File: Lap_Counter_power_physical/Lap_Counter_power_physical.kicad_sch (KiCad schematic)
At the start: 26 parts, among them J1 Panel Barrel_Jack, J11 Screw_Terminal_01x04, J18 Screw_Terminal_01x04, J2 Barrel_Jack, J3 Barrel_Plug, J4 Barrel_Jack, J5 Barrel_Plug, J6 Screw_Terminal_01x04, J7 Screw_Terminal_01x04, J8 Screw_Terminal_01x06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

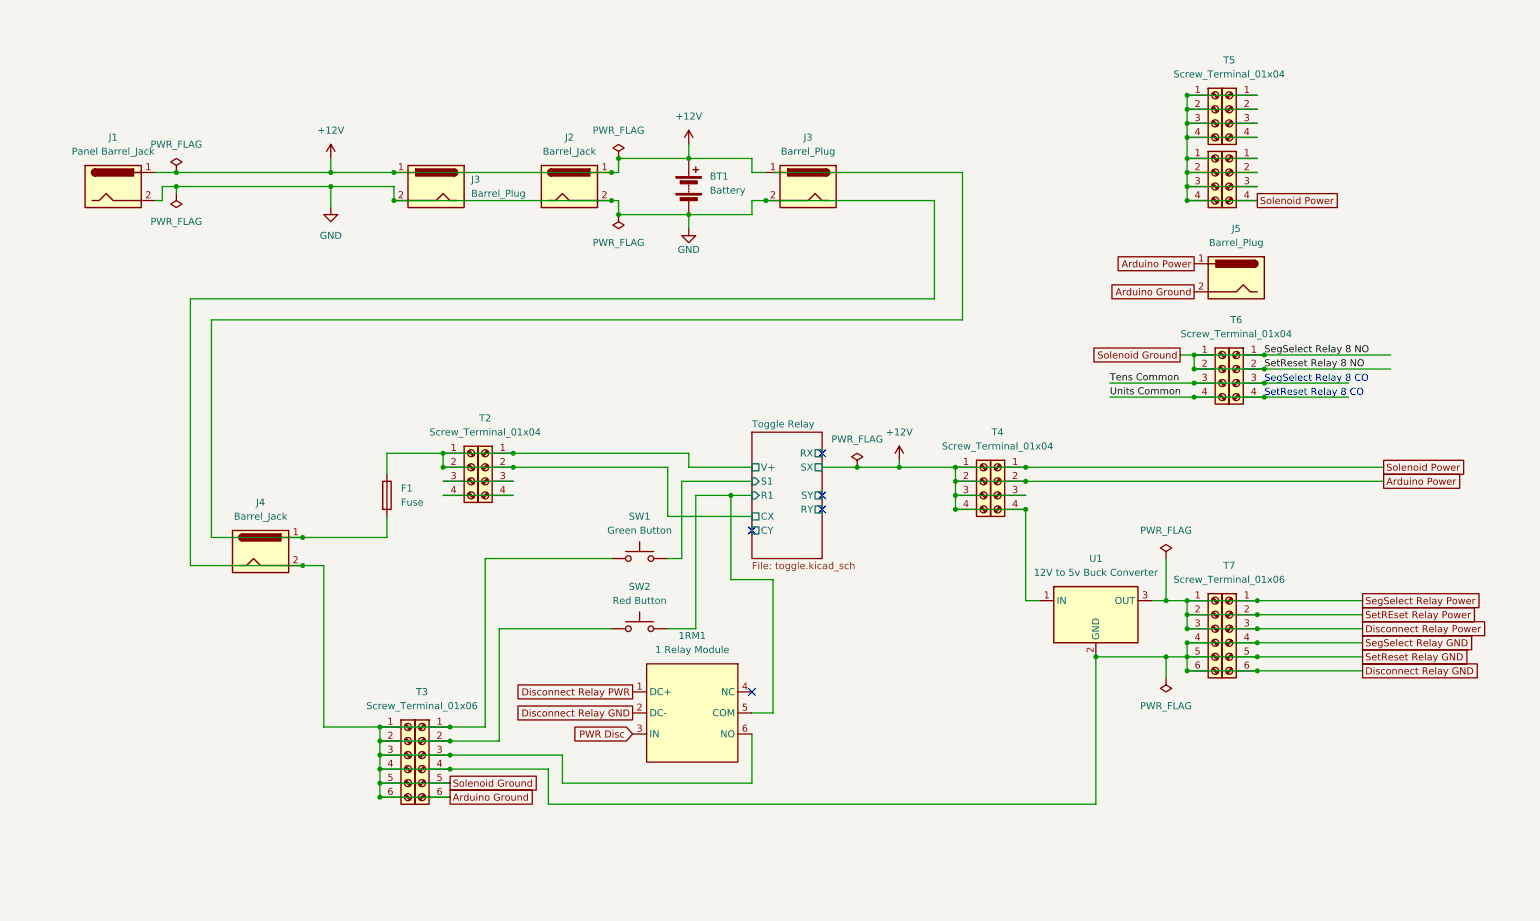
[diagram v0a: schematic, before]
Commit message: Documentation clean up and addition of spec sheets
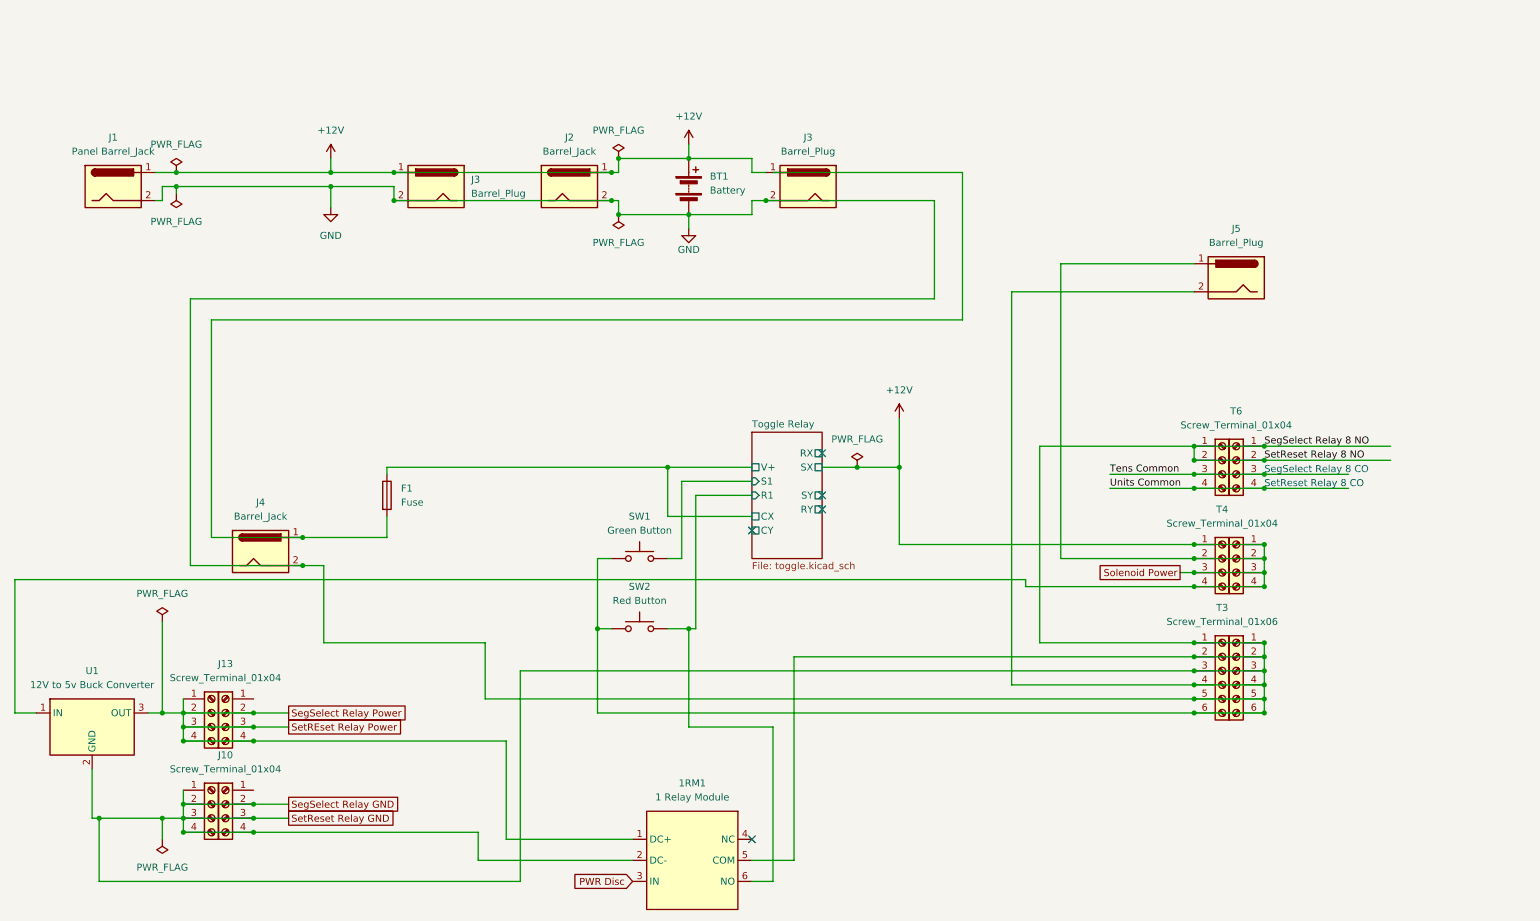
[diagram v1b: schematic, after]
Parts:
- removed J6, J7, T2, T5, T8: Screw_Terminal_01x04, symbol Connector:Screw_Terminal_01x04
- removed T7, T8: Screw_Terminal_01x06, symbol Connector:Screw_Terminal_01x06
- added J10, J12, J13: Screw_Terminal_01x04, symbol Connector:Screw_Terminal_01x04
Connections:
- net Disconnect Relay Power is gone; now on net SegSelect Relay Power: U1.3 (OUT)
- net GND: now also 1RM1.5 (COM), J9.1 (Pin_1), J9.2 (Pin_2), J9.3 (Pin_3), J9.4 (Pin_4), J10.2 (Pin_2), J10.3 (Pin_3), J10.4 (Pin_4); no longer 1RM1.6 (NO)
- net Toggle Relay/CX: no longer J9.1 (Pin_1), J9.2 (Pin_2)
- net Toggle Relay/R1: now also 1RM1.6 (NO); no longer 1RM1.5 (COM)
- net Disconnect Relay PWR renamed SegSelect Relay Power
- net SegSelect Relay Power: now also J12.1 (Pin_1), J12.2 (Pin_2), J12.3 (Pin_3), J12.4 (Pin_4), J13.2 (Pin_2), J13.3 (Pin_3), J13.4 (Pin_4)
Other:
- moved on the sheet: 1RM1, T3, T4, T6, U1

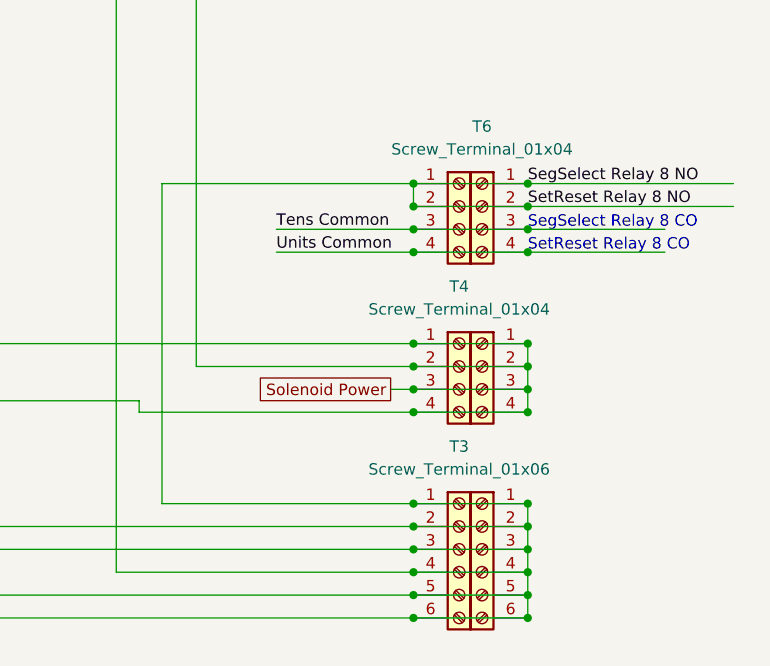
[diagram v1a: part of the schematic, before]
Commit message: eliminate over-large mp4 file
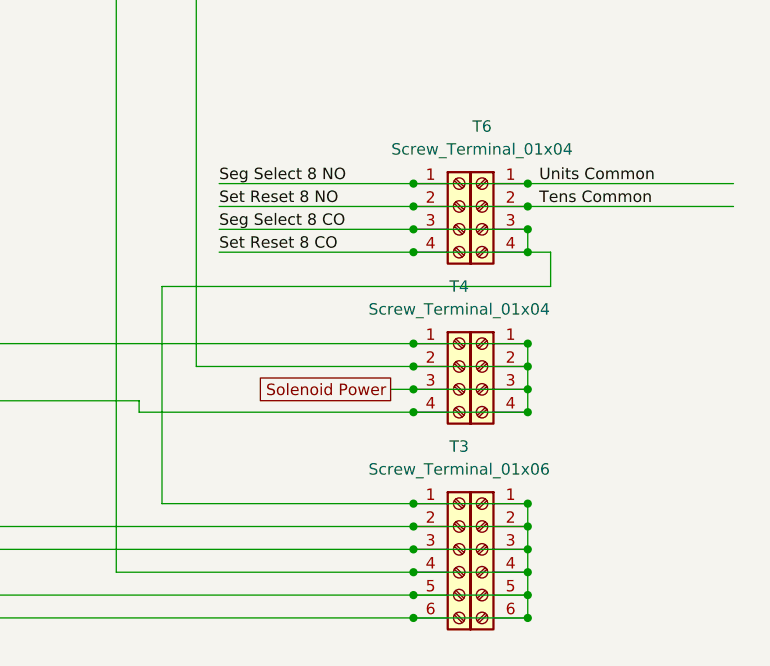
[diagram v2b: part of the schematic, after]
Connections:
- net Tens Common is gone; now on net GND: J18.3 (Pin_3), T6.3 (Pin_3)
- net Units Common is gone; now on net GND: J18.4 (Pin_4), T6.4 (Pin_4)
- net GND: no longer J18.1 (Pin_1), J18.2 (Pin_2), T6.1 (Pin_1), T6.2 (Pin_2)
- new net Seg Select 8 NO: J18.1 (Pin_1), T6.1 (Pin_1)
- new net Set Reset 8 NO: J18.2 (Pin_2), T6.2 (Pin_2)
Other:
- note removed: "SegSelect Relay 8 CO"
- note removed: "SetReset Relay 8 CO"

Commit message: Update documen
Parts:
- added DRC1: DieseRC RC Switch, symbol Project_Library:DieseRC_Remote_Control_Switch
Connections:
- net +12V: now also DRC1. (VCC)
- net GND: now also DRC1. (VCC)
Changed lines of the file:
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@@
 	)
 	(junction
+		(at 189.23 115.57)
+		(diameter 0)
+		(color 0 0 0 0)
+	)
+	(junction
 		(at 228.6 97.79)
 		(diameter 0)
@@
 	)
 	(junction
+		(at 191.77 135.89)
+		(diameter 0)
+		(color 0 0 0 0)
+	)
+	(junction
 		(at 228.6 133.35)
 		(diameter 0)
@@
 	(wire
 		(pts
-			(xy 175.26 115.57) (xy 228.6 115.57)
+			(xy 175.26 115.57) (xy 189.23 115.57)
 		)
 		(stroke
@@
 	(wire
 		(pts
+			(xy 189.23 115.57) (xy 228.6 115.57)
+		)
+		(stroke
+			(width 0)
+			(type default)
+		)
+	)
+	(wire
+		(pts
 			(xy 207.01 105.41) (xy 228.6 105.41)
 		)
@@
 	(wire
 		(pts
+			(xy 191.77 39.37) (xy 191.77 135.89)
+		)
+		(stroke
+			(width 0)
+			(type default)
+		)
+	)
+	(wire
+		(pts
 			(xy 228.6 100.33) (xy 241.3 100.33)
 		)
@@
 	(wire
 		(pts
-			(xy 156.21 135.89) (xy 228.6 135.89)
+			(xy 156.21 135.89) (xy 191.77 135.89)
 		)
 		(stroke
@@
 	(wire
 		(pts
+			(xy 191.77 135.89) (xy 228.6 135.89)
+		)
+		(stroke
+			(width 0)
+			(type default)
+		)
+	)
+	(wire
+		(pts
 			(xy 123.19 48.26) (xy 124.46 48.26)
 		)
@@
 	(wire
 		(pts
+			(xy 189.23 39.37) (xy 189.23 115.57)
+		)
+		(stroke
+			(width 0)
+			(type default)
+		)
+	)
+	(wire
+		(pts
 			(xy 123.19 53.34) (xy 124.46 53.34)
 		)
@@
 					(unit 1)
 				)
+			)
+		)
+	)
+	(symbol
+		(lib_id "Project_Library:DieseRC_Remote_Control_Switch")
+		(at 180.34 21.59 0)
+		(unit 1)
+		(exclude_from_sim no)
+		(in_bom yes)
+		(on_board yes)
+		(dnp no)
+		(fields_autoplaced yes)
+		(property "Reference" "DRC1"
+			(at 195.58 26.6699 0)
+			(effects
+				(font
+					(size 1.27 1.27)
+				)
+				(justify left)
+			)
+		)
+		(property "Value" "DieseRC RC Switch"
+			(at 195.58 29.2099 0)
+			(effects
+				(font
+					(size 1.27 1.27)
+				)
+				(justify left)
+			)
+		)
+		(property "Footprint" ""
+			(at 180.34 21.59 0)
+			(effects
+				(font
+					(size 1.27 1.27)
+				)
+				(hide yes)
+			)
+		)
+		(property "Datasheet" ""
+			(at 180.34 21.59 0)
+			(effects
+				(font
+					(size 1.27 1.27)
+				)
+				(hide yes)
+			)
+		)
+		(property "Description" ""
+			(at 180.34 21.59 0)
+			(effects
+				(font
+					(size 1.27 1.27)
+				)
+				(hide yes)
+			)
+		)
+		(pin "8"
+		)
+		(pin "1"
+		)
+		(pin "4"
+		)
+		(pin "5"
+		)
+		(pin "3"
+		)
+		(pin "11"
+		)
+		(pin "10"
+		)
+		(pin ""
+		)
+		(pin "7"
+		)
+		(pin ""
+		)
+		(pin "6"
+		)
+		(pin "2"
+		)
+		(pin "12"
+		)
+		(pin "9"
+		)
+		(instances
+			(project "Lap_Counter_power_physical"
+				(path "/78a9eac1-cabd-44e7-bd78-57e12cee5a04"
+					(reference "DRC1")
+					(unit 1)
+				)

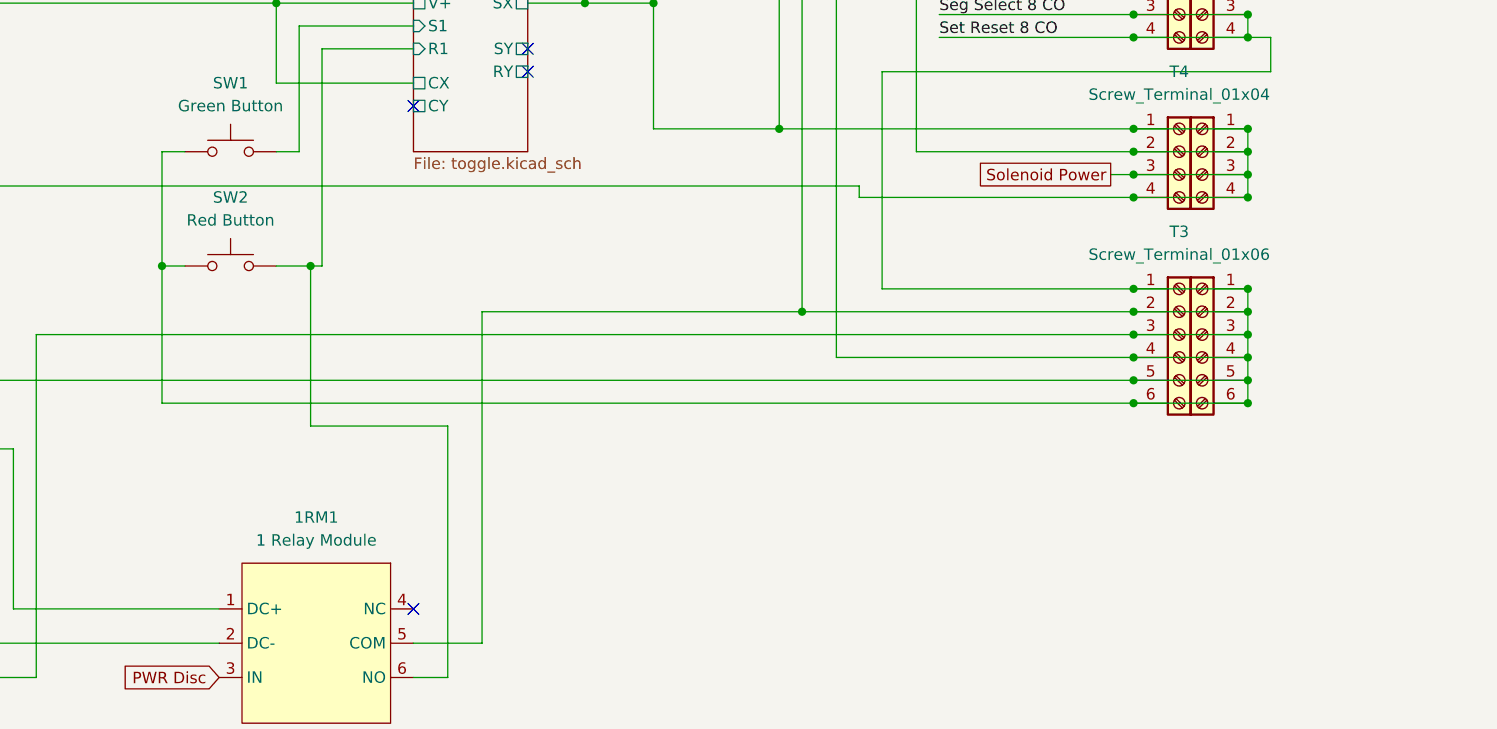
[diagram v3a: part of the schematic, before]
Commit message: Update Documentation for added regulator.
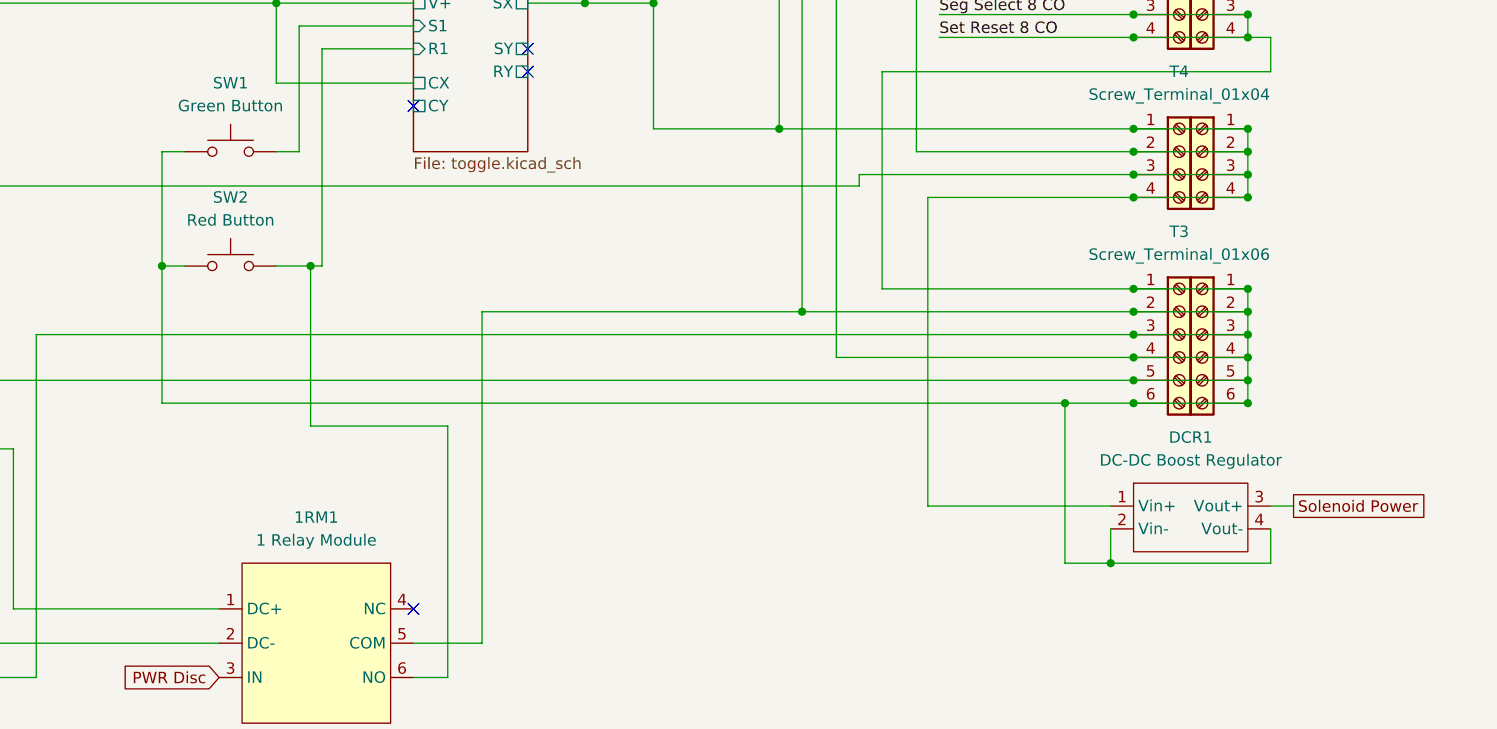
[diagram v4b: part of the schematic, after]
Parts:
- added DCR1: DC-DC Boost Regulator, symbol Project_Library:Ymiko_DC-DC_regulator
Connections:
- net +12V: now also DCR1.1 (Vin+)
- net GND: now also DCR1.2 (Vin-), DCR1.4 (Vout-)
- new net Solenoid Power: DCR1.3 (Vout+)
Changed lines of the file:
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@@
 	(paper "A4")
 	(junction
+		(at 228.6 123.19)
+		(diameter 0)
+		(color 0 0 0 0)
+	)
+	(junction
 		(at 241.3 100.33)
 		(diameter 0)
@@
 	)
 	(junction
+		(at 228.6 120.65)
+		(diameter 0)
+		(color 0 0 0 0)
+	)
+	(junction
 		(at 45.72 146.05)
 		(diameter 0)
@@
 	)
 	(junction
-		(at 228.6 120.65)
+		(at 226.06 163.83)
 		(diameter 0)
 		(color 0 0 0 0)
@@
 	)
 	(junction
-		(at 228.6 123.19)
-		(diameter 0)
-		(color 0 0 0 0)
-	)
-	(junction
 		(at 241.3 120.65)
 		(diameter 0)
@@
 	(junction
 		(at 58.42 146.05)
+		(diameter 0)
+		(color 0 0 0 0)
+	)
+	(junction
+		(at 220.98 146.05)
 		(diameter 0)
 		(color 0 0 0 0)
@@
 	(wire
 		(pts
-			(xy 120.65 146.05) (xy 228.6 146.05)
+			(xy 120.65 146.05) (xy 220.98 146.05)
 		)
 		(stroke
@@
 	(wire
 		(pts
+			(xy 226.06 163.83) (xy 243.84 163.83)
+		)
+		(stroke
+			(width 0)
+			(type default)
+		)
+	)
+	(wire
+		(pts
 			(xy 207.01 97.79) (xy 228.6 97.79)
 		)
@@
 	(wire
 		(pts
+			(xy 220.98 146.05) (xy 220.98 163.83)
+		)
+		(stroke
+			(width 0)
+			(type default)
+		)
+	)
+	(wire
+		(pts
 			(xy 241.3 115.57) (xy 228.6 115.57)
 		)
@@
 	(wire
 		(pts
+			(xy 226.06 160.02) (xy 226.06 163.83)
+		)
+		(stroke
+			(width 0)
+			(type default)
+		)
+	)
+	(wire
+		(pts
+			(xy 198.12 120.65) (xy 228.6 120.65)
+		)
+		(stroke
+			(width 0)
+			(type default)
+		)
+	)
+	(wire
+		(pts
 			(xy 175.26 92.71) (xy 175.26 101.6)
 		)
@@
 	(wire
 		(pts
+			(xy 205.74 123.19) (xy 228.6 123.19)
+		)
+		(stroke
+			(width 0)
+			(type default)
+		)
+	)
+	(wire
+		(pts
 			(xy 148.59 110.49) (xy 133.35 110.49)
 		)
@@
 	(wire
 		(pts
+			(xy 198.12 121.92) (xy 198.12 120.65)
+		)
+		(stroke
+			(width 0)
+			(type default)
+		)
+	)
+	(wire
+		(pts
 			(xy 41.91 146.05) (xy 45.72 146.05)
 		)
@@
 	(wire
 		(pts
+			(xy 205.74 157.48) (xy 226.06 157.48)
+		)
+		(stroke
+			(width 0)
+			(type default)
+		)
+	)
+	(wire
+		(pts
 			(xy 161.29 101.6) (xy 167.64 101.6)
 		)
@@
 	(wire
 		(pts
-			(xy 226.06 120.65) (xy 228.6 120.65)
-		)
-		(stroke
-			(width 0)
-			(type default)
-		)
-	)
-	(wire
-		(pts
 			(xy 241.3 135.89) (xy 241.3 138.43)
 		)
@@
 	(wire
 		(pts
+			(xy 220.98 163.83) (xy 226.06 163.83)
+		)
+		(stroke
+			(width 0)
+			(type default)
+		)
+	)
+	(wire
+		(pts
 			(xy 191.77 39.37) (xy 191.77 135.89)
 		)
@@
 	(wire
 		(pts
+			(xy 243.84 160.02) (xy 243.84 163.83)
+		)
+		(stroke
+			(width 0)
+			(type default)
+		)
+	)
+	(wire
+		(pts
 			(xy 137.16 55.88) (xy 148.59 55.88)
 		)
@@
 	(wire
 		(pts
+			(xy 205.74 157.48) (xy 205.74 123.19)
+		)
+		(stroke
+			(width 0)
+			(type default)
+		)
+	)
+	(wire
+		(pts
 			(xy 207.01 100.33) (xy 228.6 100.33)
 		)
@@
 	(wire
 		(pts
+			(xy 243.84 157.48) (xy 246.38 157.48)
+		)
+		(stroke
+			(width 0)
+			(type default)
+		)
+	)
+	(wire
+		(pts
 			(xy 83.82 53.34) (xy 123.19 53.34)
 		)
@@
 	(wire
 		(pts
+			(xy 220.98 146.05) (xy 228.6 146.05)
+		)
+		(stroke
+			(width 0)
+			(type default)
+		)
+	)
+	(wire
+		(pts
 			(xy 137.16 58.42) (xy 137.16 55.88)
 		)
@@
 	(wire
 		(pts
-			(xy 228.6 123.19) (xy 198.12 123.19)
-		)
-		(stroke
-			(width 0)
-			(type default)
-		)
-	)
-	(wire
-		(pts
 			(xy 41.91 168.91) (xy 41.91 165.1)
 		)
@@
 		(pts
 			(xy 207.01 102.87) (xy 228.6 102.87)
-		)
-		(stroke
-			(width 0)
-			(type default)
-		)
-	)
-	(wire
-		(pts
-			(xy 198.12 123.19) (xy 198.12 121.92)
 		)
 		(stroke
@@
 	(global_label "Solenoid Power"
 		(shape passive)
-		(at 226.06 120.65 180)
+		(at 246.38 157.48 0)
 		(fields_autoplaced yes)
 		(effects
@@
 				(size 1.27 1.27)
 			)
-			(justify right)
+			(justify left)
 		)
 		(property "Intersheetrefs" "${INTERSHEET_REFS}"
-			(at 209.4301 120.65 0)
-			(effects
-				(font
-					(size 1.27 1.27)
-				)
-				(justify right)
+			(at 263.0099 157.48 0)
+			(effects
+				(font
+					(size 1.27 1.27)
+				)
+				(justify left)
 				(hide yes)
 			)
@@
 					(unit 1)
 				)
+			)
+		)
+	)
+	(symbol
+		(lib_id "Project_Library:Ymiko_DC-DC_regulator")
+		(at 234.95 153.67 0)
+		(unit 1)
+		(exclude_from_sim no)
+		(in_bom yes)
+		(on_board yes)
+		(dnp no)
+		(fields_autoplaced yes)
+		(property "Reference" "DCR1"
+			(at 234.95 149.86 0)
+			(effects
+				(font
+					(size 1.27 1.27)
+				)
+			)
+		)
+		(property "Value" "DC-DC Boost Regulator"
+			(at 234.95 152.4 0)
+			(effects
+				(font
+					(size 1.27 1.27)
+				)
+			)
+		)
+		(property "Footprint" ""
+			(at 234.95 153.67 0)
+			(effects
+				(font
+					(size 1.27 1.27)
+				)
+				(hide yes)
+			)
+		)
+		(property "Datasheet" ""
+			(at 234.95 153.67 0)
+			(effects
+				(font
+					(size 1.27 1.27)
+				)
+				(hide yes)
+			)
+		)
+		(property "Description" ""
+			(at 234.95 153.67 0)
+			(effects
+				(font
+					(size 1.27 1.27)
+				)
+				(hide yes)
+			)
+		)
+		(pin "1"
+		)
+		(pin "4"
+		)
+		(pin "2"
+		)
+		(pin "3"
+		)
+		(instances
+			(project ""
+				(path "/78a9eac1-cabd-44e7-bd78-57e12cee5a04"
+					(reference "DCR1")
+					(unit 1)
+				)
